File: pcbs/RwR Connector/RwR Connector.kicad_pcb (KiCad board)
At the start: 2 copper layers, 38.1 x 127 mm, 4 parts, among them J101 Conn_02x20_Odd_Even, J102 Conn_02x20_Odd_Even, J103 Conn_01x04, J104 Conn_02x20_Odd_Even

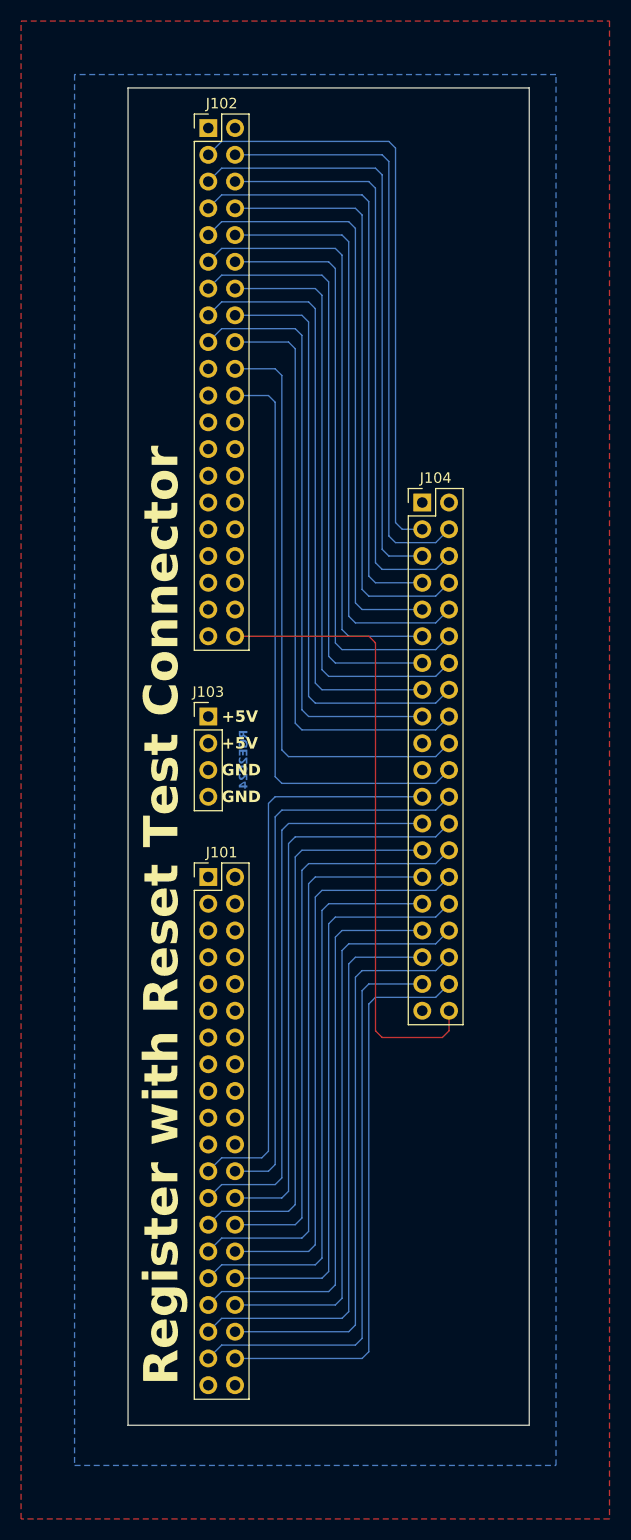
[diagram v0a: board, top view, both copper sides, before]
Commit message: Revise the Register with Reset (#3)
Updates to Register-with-Reset:

- Convert to edge connector
- Route clock through an 'AND' with the Reset line, so the clock doesn't block reset
- Shrink the board somewhat by repositioning components
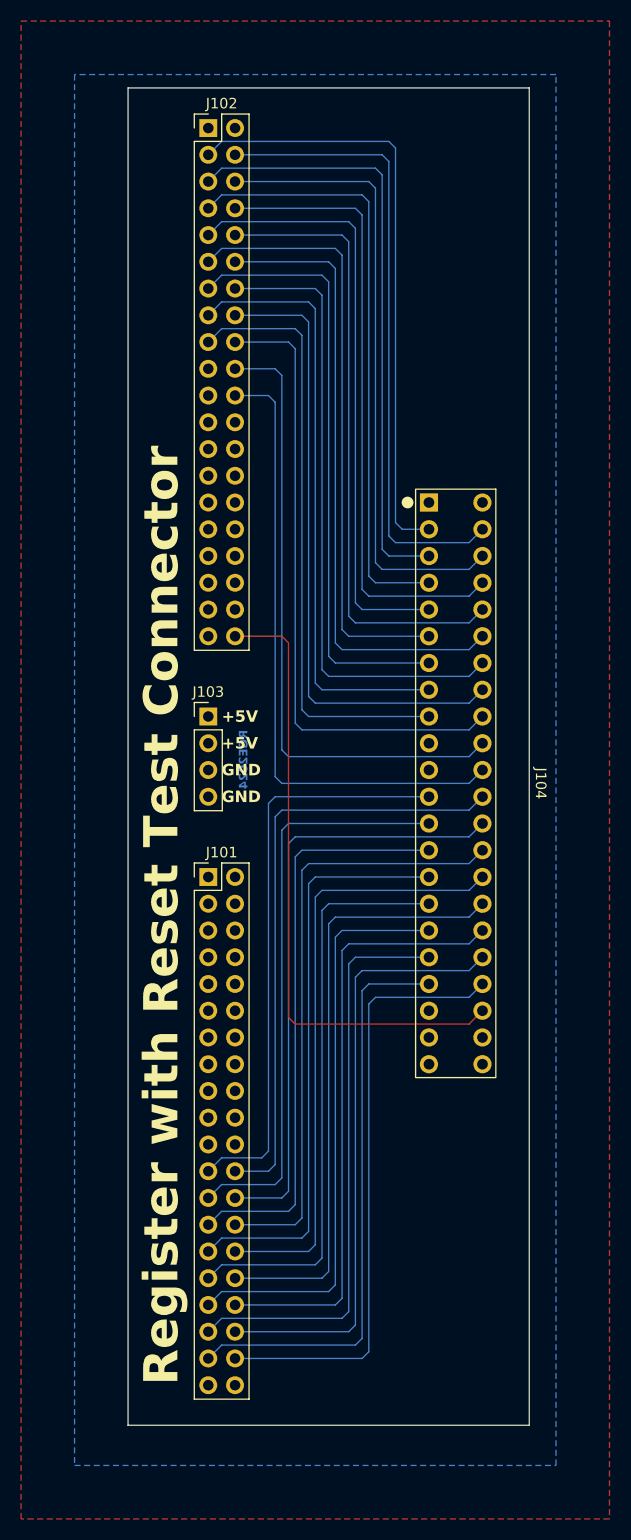
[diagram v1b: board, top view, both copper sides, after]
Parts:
- J104: value Conn_02x20_Odd_Even -> ~; footprint Connector_PinHeader_2.54mm:PinHeader_2x20_P2.54mm_Vertical -> BoardEdgeConnectors:TE-5530843-4-Mount
- moved J104 26.9 mm to (132.7, 113.0), turned to -90 degrees
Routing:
- net /Reg0.Out7: track 54.4 -> 57.6 mm
- net /~{RESET}: track 56.9 -> 60.1 mm
- net /Reg1.Out5: track 54.4 -> 57.6 mm
- net /Reg1.Out3: track 54.4 -> 57.6 mm
- net /Reg1.Out1: track 54.4 -> 57.6 mm
- net /Reg1.In7: track 56.9 -> 60.1 mm
- net /Reg1.In5: track 56.9 -> 60.1 mm
- net /Reg1.In3: track 56.9 -> 60.1 mm
- net /Reg1.In1: track 56.9 -> 60.1 mm
- net /Reg0.Out5: track 54.4 -> 57.6 mm
- net /Reg0.Out3: track 54.4 -> 57.6 mm
- net /Reg0.Out1: track 54.4 -> 57.6 mm
- net /Reg0.In7: track 56.9 -> 60.1 mm
- net /Reg0.In5: track 56.9 -> 60.1 mm
- net /Reg0.In3: track 56.9 -> 60.1 mm
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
